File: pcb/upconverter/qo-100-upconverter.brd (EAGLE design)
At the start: 100 x 70 mm, 215 parts, among them CON1 3P-SH-SIDE, CON2 2EDG-2P-5MM-H, U1 EFM32TG11B120F128GM32, U10 ADL5601, U11 F1490NLGA, U12 LTC5597, U13 2450BP15E0100, U14 DC2337J5010AHF, U15 MCP6V31, U16 MCP9802-A0, U17 SKY66292-11, U18 F1958NBGK, U19 MCP1700-330, U2 DSB321SDA, U20 LT8636, U22 MCP6C02-020, U23 ADP7142AUJZ-3.3, U24 ADP7142AUJZ-3.3, U25 ADP7142AUJZ-3.3, U26 ADM7171ACPZ-5.0, U27 ADM7172ACPZ-5.0, U3 ADF4351, U4 JSW2-63DR+, U5 2450BP15E0100, U6 F1958NBGK, U7 MAX2671, U8 2450BP15E0100, U9 F1958NBGK

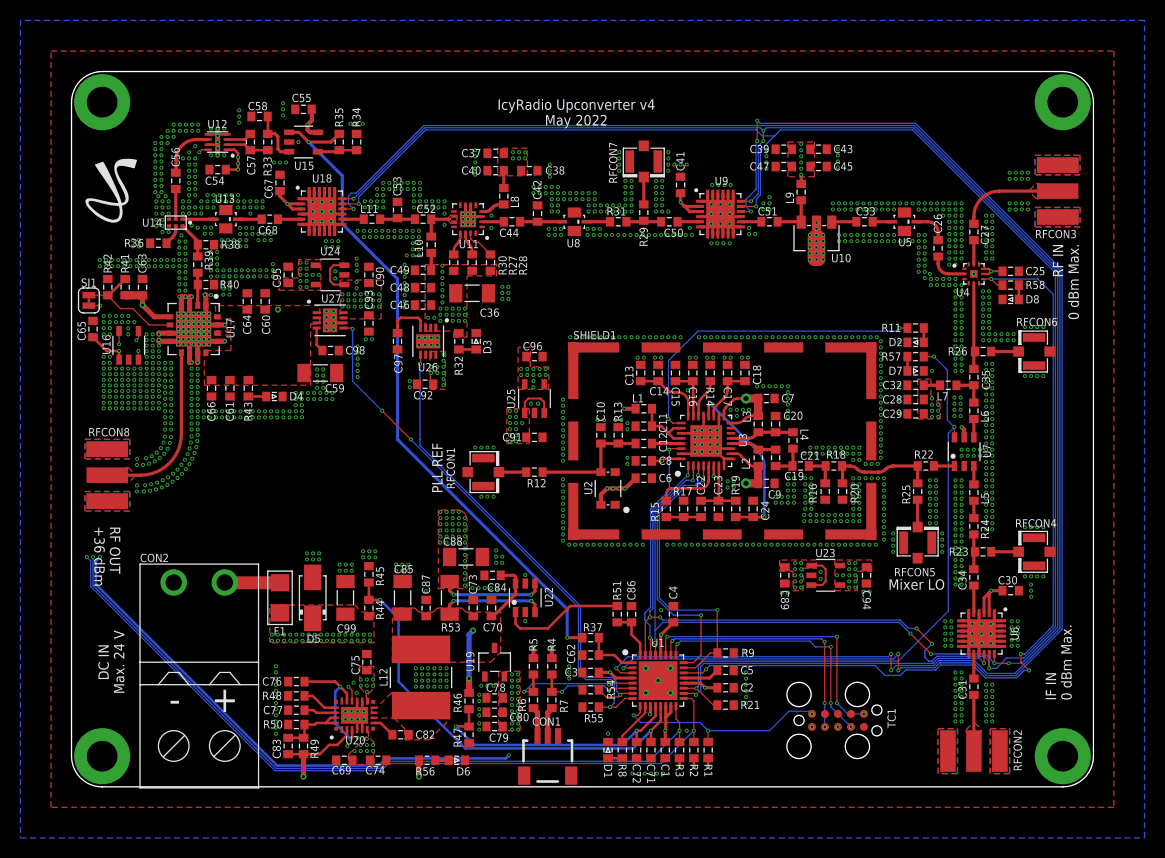
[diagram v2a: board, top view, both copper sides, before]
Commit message: Update PLL Loop filter
Signed-off-by: João Silva <jgc3silva@gmail.com>
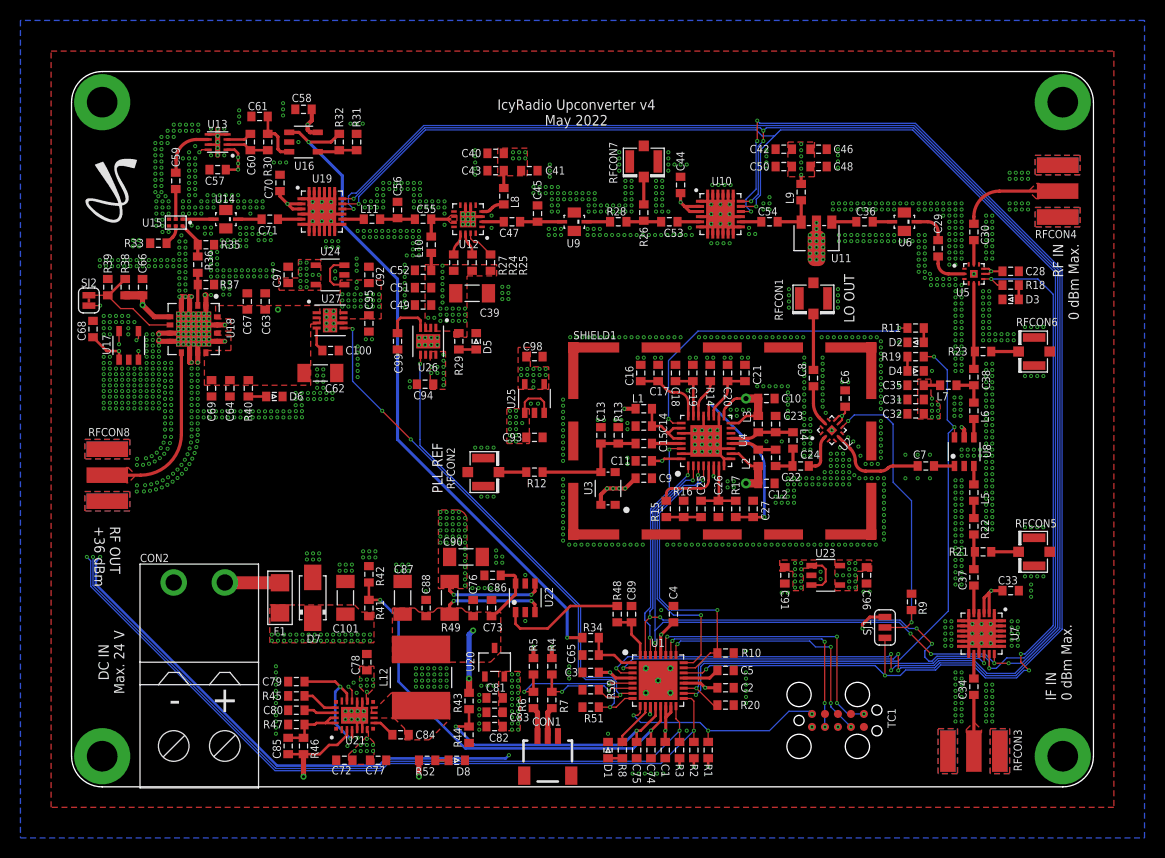
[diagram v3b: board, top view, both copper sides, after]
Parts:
- removed R53: 0.03 Ohms, Resistor:RES1206
- removed R54, R55: 100K Ohms, Resistor:RES0603
- removed R57, R58: 330 Ohms, Resistor:RES0603
- added C100: 1nF, Capacitor:CAP0603
- added C101: 10uF, Capacitor:CAP1206
- added C81: 100nF, Capacitor:CAP0603
- added R10: 100K Ohms, Resistor:RES0603
- added SJ2: SJCS, Solder Jumper:SJC_S
- added U21: LT8636, Analog Devices:QFN20_ASYM_3X4_CORNER
- C10, C12, C14, C16, C18, C44: value 10pF -> 100nF
- C13, C15, C17: value 100nF -> 10pF
- C19: value 0.7pF -> 10pF
- C20: value 0.7pF -> 100nF
- C21, C47: value 15pF -> 10pF
- C22: value 20nF -> 0.7pF
- C23: value 1nF -> 0.7pF
- C24, C71: value 470pF -> 15pF
- C25: value 100nF -> 20nF
- C26: value 15pF -> 1nF
- C27: value 15pF -> 470pF
- C28, C46, C58, C84, C89: value 1uF -> 100nF
- C29, C30, C7, C8: value 100nF -> 15pF
- C31: value 100pF -> 1uF
- C32: value 47pF -> 100nF
- C33, C51, C68: value 15pF -> 100nF
- C35: value 220pF -> 47pF
- C36, C59: value 100uF -> 15pF; device Capacitor:CAP1206 -> Capacitor:CAP0603
- C37: value 1uF -> 100pF
- C38: value 100nF -> 220pF
- C39: value 1uF -> 100uF; device Capacitor:CAP0603 -> Capacitor:CAP1206
- C40, C49: value 33pF -> 1uF
- C42: value 0.8pF -> 1uF
- C43: value 100nF -> 33pF
- C45: value 47pF -> 0.8pF
- C48: value 100nF -> 47pF
- C52: value 22pF -> 33pF
- C53: value 0.7pF -> 15pF
- C54: value 4.7uF -> 15pF
- C55: value 100nF -> 22pF
- C56: value 15pF -> 0.7pF
- C57: value 10nF -> 4.7uF
- C60, C80: value 10uF -> 10nF
- C61, C79, C94, C95: value 10uF -> 1uF
- C62: value 10nF -> 100uF; device Capacitor:CAP0603 -> Capacitor:CAP1206
- C63: value 1uF -> 10uF
- C64: value 10nF -> 10uF
- C65, C67: value 100nF -> 10nF
- C66, C77: value 10nF -> 1uF
- C69: value 4.7uF -> 10nF
- C72: value 470pF -> 4.7uF
- C73: value 4.7uF -> 100nF
- C74, C75: value 1uF -> 470pF
- C76: value 1uF -> 4.7uF
- C78, C86: value 100nF -> 1uF
- C82: value 100nF -> 10uF
- C83: value 10pF -> 10uF
- C85: value 100uF -> 10pF; device Capacitor:CAP1206 -> Capacitor:CAP0603
- C87: value 100nF -> 100uF; device Capacitor:CAP0603 -> Capacitor:CAP1206
- C88: value 22uF -> 100nF; device Capacitor:CAP1206 -> Capacitor:CAP0603
- C90: value 1uF -> 22uF; device Capacitor:CAP0603 -> Capacitor:CAP1206
- C97, C98: value 1nF -> 10uF
- C99: value 10uF -> 1nF; device Capacitor:CAP1206 -> Capacitor:CAP0603
- D5: value SMAJ24A -> LED0603; device TVS:DO214AC -> LED:0603
- D7: value LED0603 -> SMAJ24A; device LED:0603 -> TVS:DO214AC
- R16: value 105 Ohms -> 4.7K Ohms
- R17: value 330 Ohms -> 1K Ohms
- R18: value 61.9 Ohms -> 330 Ohms
- R19: value 1K Ohms -> 330 Ohms
- R20: value 105 Ohms -> 10K Ohms
- R21: value 10K Ohms -> DNP
- R24, R31: value 0 Ohms -> 1K Ohms
- R27: value 1K Ohms -> 1.5K Ohms
- R28: value DNP -> 0 Ohms
- R29: value DNP -> 510 Ohms
- R30: value 1.5K Ohms -> 0 Ohms
- R32: value 510 Ohms -> 2K Ohms
- R33: value 0 Ohms -> 49.9 Ohms
- R34: value 1K Ohms -> 100 Ohms
- R35: value 2K Ohms -> 96.1 Ohms
- R36: value 49.9 Ohms -> 71.5 Ohms
- R37: value 100 Ohms -> 96.1 Ohms
- R38: value 96.1 Ohms -> 10K Ohms
- R39: value 71.5 Ohms -> 7.5K Ohms
- R40: value 96.1 Ohms -> 510 Ohms
- R41: value 10K Ohms -> 100K Ohms
- R42: value 7.5K Ohms -> 10K Ohms
- R43: value 510 Ohms -> 100K Ohms
- R44: value 100K Ohms -> 75K Ohms
- R45: value 10K Ohms -> 41.2K Ohms
- R46: value 100K Ohms -> 1M Ohms
- R47: value 75K Ohms -> 220K Ohms
- R48: value 41.2K Ohms -> 1K Ohms
- R49: value 1M Ohms -> 0.03 Ohms; device Resistor:RES0603 -> Resistor:RES1206
- R50: value 220K Ohms -> 100K Ohms
- R51: value 1K Ohms -> 100K Ohms
- R9: value 100K Ohms -> 10K Ohms
- RFCON2: value RFCON-SMA-EDGE -> RFCON-U.FL; device RF Connector:SMA-EDGE -> RF Connector:U.FL
- RFCON4: value RFCON-U.FL -> RFCON-SMA-EDGE; device RF Connector:U.FL -> RF Connector:SMA-EDGE
- SJ1: value SJCS -> (none); device Solder Jumper:SJC_S -> Solder Jumper:SJ2_S
- U10: value ADL5601 -> F1958NBGK; device Analog Devices:SOT89 -> Renesas:QFN24_2
- U11: value F1490NLGA -> ADL5601; device Renesas:QFN16 -> Analog Devices:SOT89
- U12: value LTC5597 -> F1490NLGA; device Analog Devices:DFN8_2X2 -> Renesas:QFN16
- U13: value 2450BP15E0100 -> LTC5597; device Generic Filter:2450BP15E0100 -> Analog Devices:DFN8_2X2
- U14: value DC2337J5010AHF -> 2450BP15E0100; device Anaren:DC2337J5010AHF -> Generic Filter:2450BP15E0100
- U15: value MCP6V31 -> DC2337J5010AHF; device Microchip:SOT23-5 -> Anaren:DC2337J5010AHF
- U16: value MCP9802-A0 -> MCP6V31
- U17: value SKY66292-11 -> MCP9802-A0; device Skyworks:SKY66292-11 -> Microchip:SOT23-5
- U18: value F1958NBGK -> SKY66292-11; device Renesas:QFN24_2 -> Skyworks:SKY66292-11
- U19: value MCP1700-330 -> F1958NBGK; device Microchip:SOT23 -> Renesas:QFN24_2
- U2: value DSB321SDA -> JSW2-63DR+; device Crystal:TCXO-3225 -> Mini Circuits:MT1818
- U20: value LT8636 -> MCP1700-330; device Analog Devices:QFN20_ASYM_3X4_CORNER -> Microchip:SOT23
- U3: value ADF4351 -> DSB321SDA; device Analog Devices:QFN32 -> Crystal:TCXO-3225
- U4: value JSW2-63DR+ -> ADF4351; device Mini Circuits:MT1818 -> Analog Devices:QFN32
- U5: value 2450BP15E0100 -> JSW2-63DR+; device Generic Filter:2450BP15E0100 -> Mini Circuits:MT1818
- U6, U9: value F1958NBGK -> 2450BP15E0100; device Renesas:QFN24_2 -> Generic Filter:2450BP15E0100
- U7: value MAX2671 -> F1958NBGK; device Maxim Integrated:SOT23-6 -> Renesas:QFN24_2
- U8: value 2450BP15E0100 -> MAX2671; device Generic Filter:2450BP15E0100 -> Maxim Integrated:SOT23-6
- moved SJ1 84.2 mm to (79.6, 15.6), turned to 90 degrees
- moved D8 70.5 mm to (37.7, 2.60), turned to 180 degrees
- moved C71 64.0 mm to (19.4, 55.5), turned to 180 degrees
- moved D7 63.0 mm to (23.6, 18.5), turned to 90 degrees
- moved D4 62.8 mm to (82.6, 40.7)
- moved C37 62.5 mm to (88.3, 20.5), turned to 90 degrees
- moved C65 58.2 mm to (50.8, 12.9), turned to 180 degrees
- moved R24 55.5 mm to (39.2, 51.3)
- moved RFCON3 55.4 mm to (88.3, 3.50), turned to 0 degrees
- moved RFCON2 55.2 mm to (40.3, 30.8)
- moved C54 54.2 mm to (68.3, 55.3)
- moved R34 53.6 mm to (50.8, 14.6), turned to 180 degrees
- moved D3 52.5 mm to (91.9, 47.7), turned to 0 degrees
- moved R37 51.1 mm to (13.2, 49.1)
- moved C38 48.0 mm to (88.3, 40.1), turned to 90 degrees
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- renumbered R56 to R52
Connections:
- removed net N$29: C21.2, R16.2, R18.2
- removed net N$45: R22.2, U7.1
- removed net N$47: R25.1, RFCON5.P$3
- new net LO_OUT: C8.1, RFCON1.P$3
- new net LO_SW_CTL: R9.2, SJ1.2, U2.7
- new net N$10: C7.1, U2.5
- new net N$14: C8.2, U2.11
- new net SYNTH_OUT: C24.2, U2.2
- net !MIXER_SHDN: now also R19.2, R20.2, U8.6; no longer R21.2, R57.2, U7.6
- net 3V3: now also C68.1, C81.1, C82.1, C83.1, SJ1.3, U17.1, U20.2; no longer C65.1, C78.1, C79.1, C80.1, U16.1, U19.2
- net 3V3_IF_ATT_MIXER_SW_CLEAN: now also C31.1, C33.1, C35.1, C96.1, U5.8, U5.9, U7.2, U7.3, U8.5; no longer C25.1, C29.1, C30.1, C94.1, U4.8, U4.9, U6.2, U6.3, U7.5
- net 3V3_PLL_CLEAN: now also C10.1, C11.1, C12.1, C98.1, U2.8, U2.9, U3.4, U4.10, U4.16, U4.17, U4.32, U4.6; no longer C7.1, C8.1, C96.1, U2.4, U3.10, U3.16, U3.17, U3.32, U3.6
- net 3V3_RF_ATT_PDET_CLEAN: now also C44.1, C57.1, C58.1, C70.1, C97.1, U10.2, U10.3, U13.1, U13.8, U16.5, U19.2, U19.3; no longer C41.1, C54.1, C55.1, C67.1, C95.1, U12.1, U12.8, U15.5, U18.2, U18.3, U9.2, U9.3
- net 5V0: now also C76.1, C86.1, C88.1, R43.2, U20.3, U21.2; no longer C70.1, C83.1, C84.1, R53.2, U19.3, U20.2
- net 5V0_BST: now also C84.2, U21.7; no longer C82.2, U20.7
- net 5V0_FB: now also C85.2, R46.1, R47.2, U21.19, U21.20; no longer C83.2, R49.1, R50.2, U20.19, U20.20
- net 5V0_INTVCC: now also C79.1, U21.15, U21.3; no longer C76.1, U20.15, U20.3
- net 5V0_ISENSE: now also C94.1, C95.1, R49.1; no longer C88.1, C89.1, R53.1
- net 5V0_PA_STG1_2_CLEAN: now also C41.1, C42.1, C50.1, C51.1, C52.1, R24.2, R25.2, R29.2; no longer C36.1, C37.1, C38.1, C45.1, C47.1, R28.2, R30.2, R32.2
- net 5V0_PA_STG3_CLEAN: now also C62.1, C67.1, C69.1, R38.2, R40.2, U18.12, U18.14, U18.16, U18.5; no longer C59.1, C60.1, C61.1, R41.2, R43.2, U17.12, U17.14, U17.16, U17.5
- net 5V0_RT: now also R45.2, U21.17; no longer R48.2, U20.17
- net 5V0_SS: now also C80.1, U21.18; no longer C77.1, U20.18
- net 5V0_SW: now also C84.1, U21.10, U21.8, U21.9; no longer C82.1, U20.10, U20.8, U20.9
- net 5V0_VSENSE: now also C75.1, R43.1, R44.2; no longer C72.1, R46.1, R47.2
- net GND: now also C100.2, C101.2, C12.2, C19.2, C21.2, C26.2, C27.2, C31.2, C33.2, C35.2, C44.2, C50.2, C51.2, C52.2, C56.2, C57.2, C68.2, C81.2, C82.2, C83.2, D5.C, D7.A, R10.1, R31.1, R33.1, R35.1, R37.1, R39.1, R44.1, R51.1, RFCON2.P$1, RFCON2.P$2, RFCON4.GND@0, RFCON4.GND@1, RFCON4.GND@2, RFCON4.GND@3, U10.1, U10.10, U10.11, U10.12, U10.13, U10.15, U10.19, U10.20, U10.21, U10.22, U10.23, U10.24, U10.25, U10.6, U10.7, U10.8, U10.9, U11.2, U11.4, U12.1, U12.12, U12.17, U12.3, U12.6, U12.8, U13.4, U13.5, U13.7, U13.9, U14.1, U15.3, U15.4, U17.2, U18.17, U18.3, U19.10, U19.11, U19.12, U19.13, U19.15, U19.19, U19.20, U19.21, U19.22, U19.23, U19.24, U19.25, U19.4, U19.6, U19.7, U19.8, U19.9, U2.10, U2.12, U2.17, U2.3, U2.4, U2.6, U20.1, U21.12, U21.13, U21.21, U21.4, U21.5, U21.M1, U21.M2, U21.M3, U21.M4, U3.1, U3.2, U4.11, U4.14, U4.15, U4.18, U4.21, U4.27, U4.31, U4.33, U4.8, U4.9, U5.10, U5.12, U5.17, U5.4, U5.6, U6.3, U7.1, U7.10, U7.11, U7.12, U7.13, U7.15, U7.19, U7.20, U7.21, U7.22, U7.23, U7.24, U7.25, U7.4, U7.6, U7.7, U7.8, U7.9, U8.2, U9.3; no longer C15.2, C24.2, C25.2, C29.2, C30.2, C36.2, C37.2, C38.2, C47.2, C53.2, C54.2, C55.2, C59.2, C60.2, C7.2, C71.2, C8.2, C84.2, C85.2, D5.A, D7.C, R17.1, R21.1, R34.1, R36.1, R38.1, R40.1, R48.1, R54.1, R55.1, RFCON2.GND@0, RFCON2.GND@1, RFCON2.GND@2, RFCON2.GND@3, RFCON4.P$1, RFCON4.P$2, U10.2, U11.1, U11.12, U11.17, U11.3, U11.5, U11.6, U11.7, U11.8, U11.9, U12.4, U13.1, U13.3, U14.4, U15.2, U17.1, U17.10, U17.11, U17.13, U17.15, U17.17, U17.3, U17.4, U17.7, U17.8, U18.12, U18.19, U18.20, U18.21, U18.22, U18.23, U18.24, U18.25, U18.6, U18.9, U2.2, U20.12, U20.13, U20.21, U20.4, U20.5, U20.M1, U20.M2, U20.M3, U20.M4, U3.11, U3.14, U3.15, U3.18, U3.21, U3.27, U3.31, U3.33, U3.8, U3.9, U4.1, U4.10, U4.12, U4.17, U4.3, U4.4, U4.6, U6.10, U6.11, U6.12, U6.13, U6.15, U6.19, U6.20, U6.21, U6.22, U6.23, U6.24, U6.25, U6.4, U6.6, U6.7, U6.8, U6.9, U7.2, U8.1, U8.3, U9.10, U9.11, U9.12, U9.13, U9.15, U9.19, U9.20, U9.21, U9.22, U9.23, U9.24, U9.25, U9.4, U9.6, U9.7, U9.8, U9.9
- net I2C1_SCL: now also U17.4; no longer U16.4
- net I2C1_SDA: now also U17.5; no longer U16.5
- net IF_ATT_ACC: now also R22.1; no longer R24.1
- net IF_ATT_ACC_PROBE: now also C37.2, R21.1, R22.2; no longer C34.2, R23.1, R24.2
- net IF_ATT_DCC: now also C37.1, U7.5; no longer C34.1, U6.5
- net IF_ATT_LE: now also U7.16; no longer U6.16
- net IF_IN_ACC: now also C34.2, U7.14; no longer C31.2, U6.14
- net IF_IN_DCC: now also C34.1, RFCON3.SIG; no longer C31.1, RFCON2.SIG
- net MIXER_IN_DCC: now also U8.3; no longer U7.3
- net MIXER_LO: now also C7.2, U8.1; no longer R18.1, R20.2, R22.1, R25.2
- net MIXER_OUT_ACC: now also C38.2, R23.1, U5.5; no longer C35.2, R26.1, U4.5
- net MIXER_OUT_DCC: now also U8.4; no longer U7.4
- net N$1: now also C22.2, C24.1; no longer C19.2, C21.1
- net N$12: now also U12.4; no longer U11.4
- net N$149: now also D8.A; no longer D6.A
- net N$15: now also R24.1, U12.14; no longer R27.1, U11.14
- net N$16: now also R27.1, U12.13; no longer R30.1, U11.13
- net N$2: now also C100.1; no longer C98.1
- net N$20: now also C99.1; no longer C97.1
- net N$21: now also RFCON2.P$3; no longer RFCON1.P$3
- net N$23: now also D5.A, R29.1; no longer D3.A, R32.1
- net N$24: now also R21.2, RFCON5.P$3; no longer R23.2, RFCON4.P$3
- net N$28: now also R23.2; no longer R26.2
- net N$3: now also D6.A, R40.1; no longer D4.A, R43.1
- net N$30: now also C47.2, U12.2; no longer C44.2, U11.2
- net N$35: now also R26.2; no longer R29.2
- net N$39: now also U19.14; no longer U18.14
- net N$4: now also R25.1, U12.15; no longer R28.1, U11.15
- net N$42: now also R33.2, U15.5; no longer R36.2, U14.5
- net N$43: now also C59.1, U13.6; no longer C56.1, U12.6
- net N$44: now also C60.2, U13.3; no longer C57.2, U12.3
- net N$5: now also D4.A, R19.1; no longer D7.A, R57.1
- net N$6: now also C38.1; no longer C35.1
- net N$67: now also C23.1, U4.13; no longer C20.1, U3.13
- net N$69: now also C22.1, U4.12; no longer C19.1, U3.12
- net N$7: now also R31.2, R32.2, U16.4; no longer R34.2, R35.2, U15.4
- net N$8: now also C14.1, U4.26, U4.28; no longer C11.1, U3.26, U3.28
- net N$84: now also C25.2, R16.2; no longer C22.2, R17.2
- net N$88: now also U4.22; no longer U3.22
- net N$9: now also D3.A, R18.1; no longer D8.A, R58.1
- net PA3_EN: now also R38.1, R39.2, SJ2.1, U18.6; no longer R41.1, R42.2, SJ1.1, U17.6
- net PA_STG1_2_BIAS_EN: now also R50.2; no longer R54.2
- net PA_STG3_BIAS_EN: now also R51.2; no longer R55.2
- net PA_TEMP_ALERT: now also SJ2.2, U17.3; no longer SJ1.2, U16.3
- net PLL_CP_VOUT: now also C25.1, C26.1, R17.2, U4.7; no longer C22.1, C23.1, R19.2, U3.7
- net PLL_EN: now also R10.2, U4.4; no longer R9.2, U3.4
- net PLL_FASTLOCK_SW: now also U4.5; no longer U3.5
- net PLL_LE: now also U4.3; no longer U3.3
- net PLL_LOCK: now also U4.25; no longer U3.25
- net PLL_MUXOUT: now also U4.30; no longer U3.30
- net PLL_REF_ACC: now also C15.2, U4.29; no longer C12.2, U3.29
- net PLL_REF_DCC: now also C13.1, C15.1, U3.3; no longer C10.1, C12.1, U2.3
- net PLL_TEMP: now also C20.1, C21.1, U4.19; no longer C17.1, C18.1, U3.19
- net PLL_VCOM: now also C18.1, C19.1, U4.23; no longer C15.1, C16.1, U3.23
- net PLL_VREF: now also C16.1, C17.1, U4.24; no longer C13.1, C14.1, U3.24
- net PLL_VTUNE: now also C27.1, R17.1, U4.20; no longer C24.1, R19.1, U3.20
- net RF_ATT1_LE: now also U10.16; no longer U9.16
- net RF_ATT2_LE: now also U19.16; no longer U18.16
- net RF_FINAL_ACC: now also U18.9; no longer U17.9
- net RF_FLT_ACC: now also C36.2, U11.1; no longer C33.2, U10.1
- net RF_IN_ACC: now also C30.2, U5.11; no longer C27.2, U4.11
- net RF_IN_DCC: now also C30.1, RFCON4.SIG; no longer C27.1, RFCON3.SIG
- net RF_PRE1_ACC: now also C54.2, U10.14; no longer C51.2, U9.14
- net RF_PRE1_ATT_ACC: now also R28.1, U9.4; no longer R31.1, U8.4
- net RF_PRE1_ATT_ACC_PROBE: now also C53.2, R26.1, R28.2; no longer C50.2, R29.1, R31.2
- net RF_PRE1_ATT_DCC: now also C53.1, U10.5; no longer C50.1, U9.5
- net RF_PRE1_ATT_FLT_ACC: now also C45.1, C47.1, U9.2; no longer C42.1, C44.1, U8.2
- net RF_PRE1_DCC: now also C54.1, U11.3; no longer C51.1, U10.3
- net RF_PRE2_ACC: now also C55.2, C56.1; no longer C52.2, C53.1
- net RF_PRE2_ATT_ACC: now also C71.2, U14.4; no longer C68.2, U13.4
- net RF_PRE2_ATT_DCC: now also C71.1, U19.5; no longer C68.1, U18.5
- net RF_PRE2_ATT_FLT_ACC: now also U14.2, U15.1; no longer U13.2, U14.1
- net RF_PRE2_ATT_FLT_CPL_ACC: now also C59.2, U15.2; no longer C56.2, U14.2
- net RF_PRE2_ATT_FLT_THRU_ACC: now also R35.2, R36.2, U15.6; no longer R38.2, R39.2, U14.6
- net RF_PRE2_ATT_FLT_THRU_ACC_ATT: now also R36.1, R37.2, U18.2; no longer R39.1, R40.2, U17.2
- net RF_PRE2_DCC: now also C55.1, U12.10, U12.11; no longer C52.1, U11.10, U11.11
- net RF_SEL_ACC: now also C29.2, U6.4; no longer C26.2, U5.4
- net RF_SEL_DCC: now also C29.1, U5.2; no longer C26.1, U4.2
- net RF_SEL_FILT_DCC: now also C36.1, U6.2; no longer C33.1, U5.2
- net RF_SW_CTL: now also R18.2, SJ1.1, U5.7; no longer R58.2, U4.7
- net SPI_MOSI: now also U10.18, U19.18, U4.2, U7.18; no longer U18.18, U3.2, U6.18, U9.18
- net SPI_SCK: now also U10.17, U19.17, U4.1, U7.17; no longer U18.17, U3.1, U6.17, U9.17
- net V5V0_ISENSE: now also C89.1, R48.1; no longer C86.1, R51.1
- net V5V0_ISENSE-AMP: now also R48.2; no longer R51.2
- net VIN: now also C101.1, C72.1, C77.1, C78.1, D7.C, R41.2, U21.11, U21.14, U21.6; no longer C69.1, C74.1, C75.1, C99.1, D5.C, R44.2, U20.11, U20.14, U20.6
- net VIN_VSENSE: now also C74.1, R41.1, R42.2; no longer C71.1, R44.1, R45.2
- net VPDET_AMP: now also R32.1, R34.2, U16.1; no longer R35.1, R37.2, U15.1
- net VPDET_FLT: now also C61.1, R30.1, U16.3; no longer C58.1, R33.1, U15.3
- net VPDET_RAW: now also C60.1, R30.2, U13.2; no longer C57.1, R33.2, U12.2
- net VPDET_SENSE: now also C65.1, R34.1; no longer C62.1, R37.1
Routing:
- net LO_SW_CTL: track 0.00 -> 30.0 mm, vias 0 -> 2
- net N$10: track 0.00 -> 9.53 mm
- net MIXER_LO: track 11.1 -> 2.00 mm
- net 3V3: track 98.3 -> 106.5 mm, vias 34 -> 35
- net LO_OUT: track 0.00 -> 5.48 mm
- net N$14: track 0.00 -> 3.99 mm
- net SYNTH_OUT: track 0.00 -> 3.82 mm
- net RF_SW_CTL: track 83.2 -> 86.9 mm, vias 4 -> 5
- net N$29: track 3.38 -> 0.00 mm
- net 3V3_PLL_CLEAN: track 25.1 -> 28.0 mm, vias 21 -> 22
- net N$47: track 2.68 -> 0.00 mm
- net N$45: track 2.00 -> 0.00 mm
- net GND: vias 1718 -> 1720
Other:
- board text added: "LO OUT"
- board text removed: "Mixer LO"
